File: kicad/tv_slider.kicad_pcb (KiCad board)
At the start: 2 copper layers, 100.6 x 75.2 mm, 95 parts, among them J1 MC 1,5/2-G-3.81, J2 MC 1,5/6-G-3.81, J3 MC 1,5/4-G-3.81, J4 MC 1,5/3-G-3.81, J5 MC 1,5/3-G-3.81, J6 MC 1,5/3-G-3.81, J7 MC 1,5/3-G-3.81, J8 Conn_01x04, Q1 CSD19537Q3, Q2 BSS138, U1 TPS26632RGE, U2 LMR33610ADDAR, U3 LMR33610ADDAR, U4 ESP32-C6-DEVKITC-1-N8, U6 ISL3280ExHZ, U7 LS7184N-S, U8 ISL3280ExHZ, U9 DRV8452SPWPR

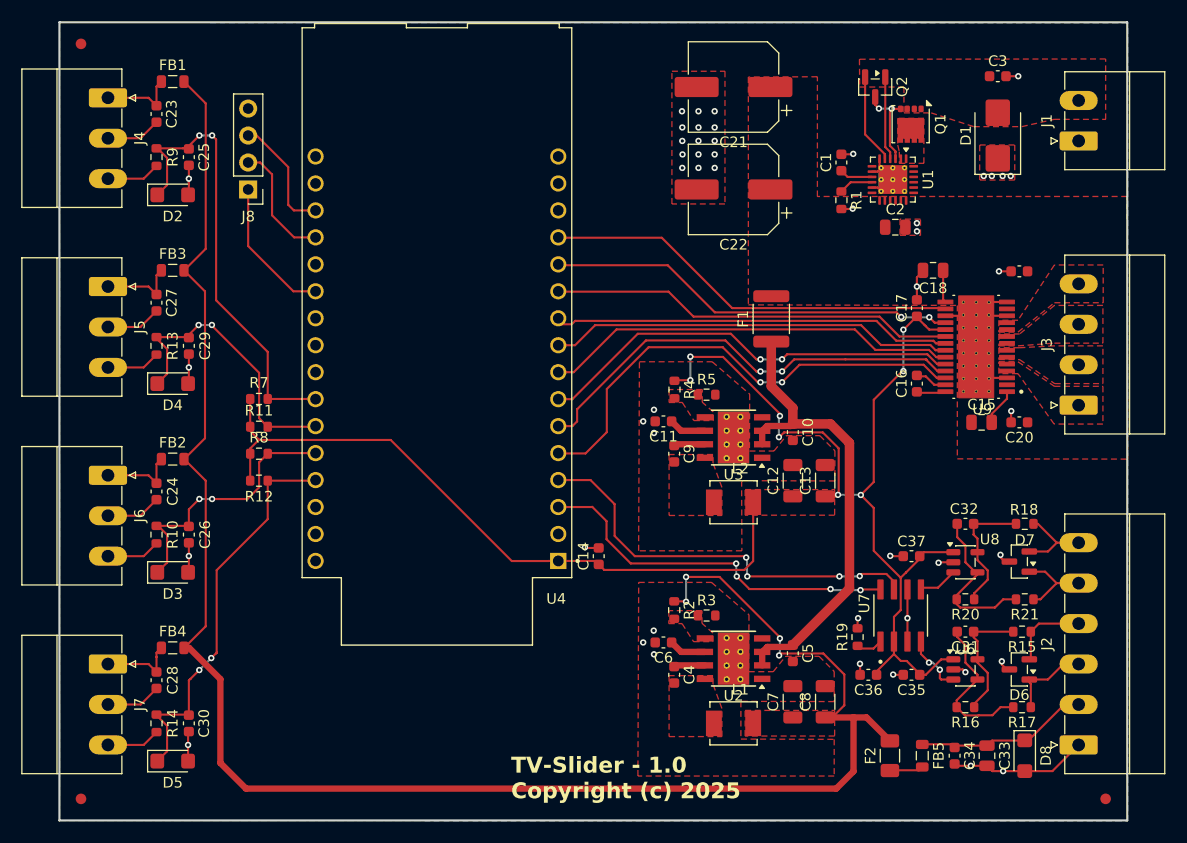
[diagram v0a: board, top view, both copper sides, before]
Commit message: Re-annotated and added extra capacitors for the 5V and 3V3 DC-DC converters. Added testpoints to the electronic fuse.
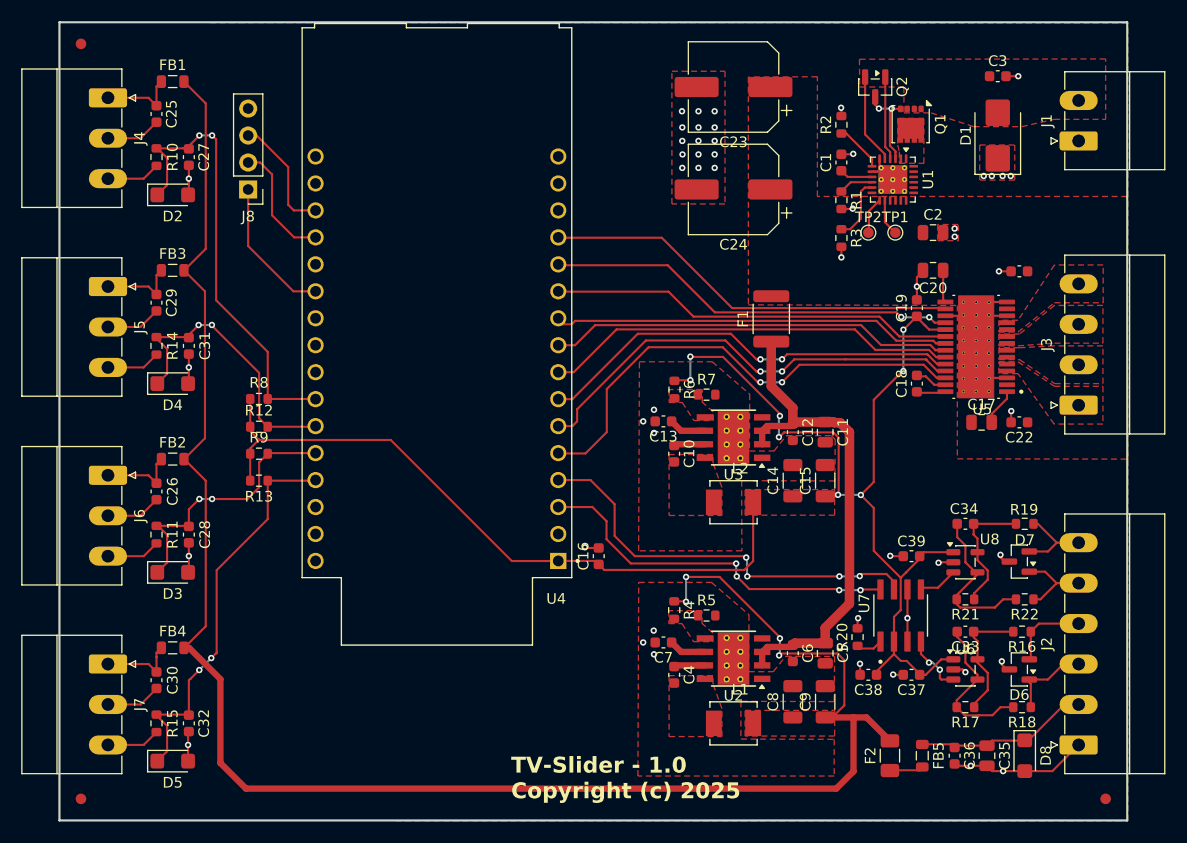
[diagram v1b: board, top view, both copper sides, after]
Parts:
- added C11: 4.7u, Capacitor_SMD:C_0805_2012Metric, F.Cu at (153.9, 95.0)
- added C5: 4.7u, Capacitor_SMD:C_0805_2012Metric, F.Cu at (153.9, 115.8)
- added R2: 0, Resistor_SMD:R_0603_1608Metric, F.Cu at (155.4, 66.0)
- added R3: 0, Resistor_SMD:R_0603_1608Metric, F.Cu at (155.4, 76.7)
- added TP1: ~{FLT}, TestPoint:TestPoint_Pad_D1.0mm, F.Cu at (160.5, 76.2)
- added TP2: IMON, TestPoint:TestPoint_Pad_D1.0mm, F.Cu at (158.0, 76.2)
- F1: value 300mA -> 100mA
- R1: value 6.98k -> 9.09k
- moved C2 3.59 mm to (164.1, 76.2)
- renumbered C9 to C10, C10 to C12, C11 to C13, C12 to C14, C13 to C15, C14 to C16, C15 to C17, C16 to C18, C17 to C19, C18 to C20, C19 to C21, C20 to C22, C21 to C23, C22 to C24, C23 to C25, C24 to C26, C25 to C27, C26 to C28, C27 to C29, C28 to C30, C29 to C31, C30 to C32, C31 to C33, C32 to C34, C33 to C35, C34 to C36, C35 to C37, C36 to C38, C37 to C39, C5 to C6, C6 to C7, C7 to C8, C8 to C9, R9 to R10, R10 to R11, R11 to R12, R12 to R13, R13 to R14, R14 to R15, R15 to R16, R16 to R17, R17 to R18, R18 to R19, R19 to R20, R20 to R21, R21 to R22, R2 to R4, R3 to R5, R4 to R6, R5 to R7, R7 to R8, R8 to R9, U9 to U5
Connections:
- U1 pad 11: GND -> Net-(U1-MODE)
- U1 pad 13: unconnected-(U1-IMON-Pad13) -> Net-(U1-IMON)
- U1 pad 14: unconnected-(U1-~{FLT}-Pad14) -> Net-(U1-~{FLT})
- U1 pad 7: unconnected-(U1-PLIM-Pad7) -> Net-(U1-PLIM)
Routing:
- net Net-(U1-MODE): track 0.00 -> 6.00 mm
- net Net-(U1-PLIM): track 0.00 -> 4.56 mm
- net Net-(U1-IMON): track 0.00 -> 3.47 mm
- net Net-(U1-~{FLT}): track 0.00 -> 3.44 mm
- net Net-(U2-EN): track 44.8 -> 47.2 mm
- net +5V: track 173.1 -> 173.8 mm
- net GND: track 80.0 -> 80.7 mm, vias 49 -> 51
- net +3V3: track 153.6 -> 154.2 mm

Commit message: Fixed up or explained all DRC violations.
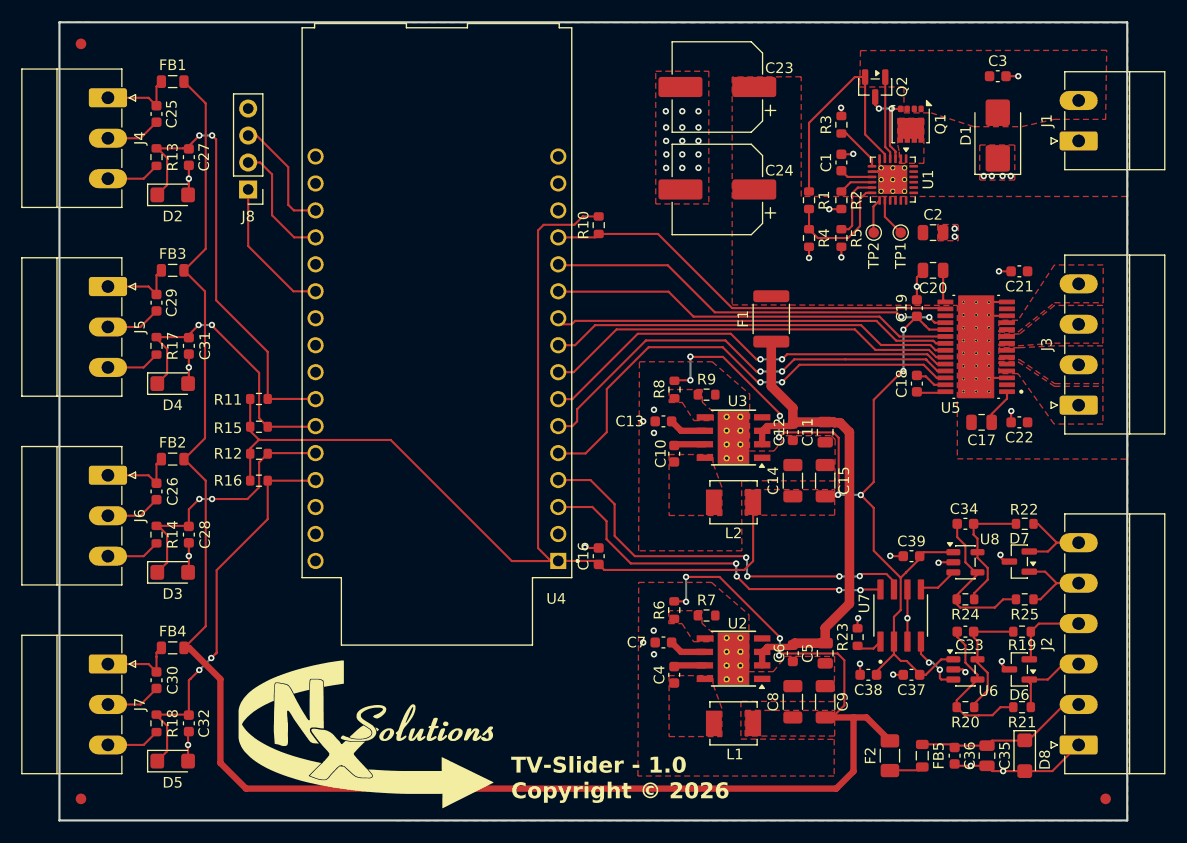
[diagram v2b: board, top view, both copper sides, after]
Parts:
- added R1: 1M, Resistor_SMD:R_0603_1608Metric, F.Cu at (152.4, 73.2)
- added R10: 10k, Resistor_SMD:R_0603_1608Metric, F.Cu at (132.6, 75.5)
- added R4: 150k, Resistor_SMD:R_0603_1608Metric, F.Cu at (152.4, 76.7)
- moved C23 1.52 mm to (143.8, 62.5)
- moved C24 1.52 mm to (143.8, 72.1)
- moved TP1 0.51 mm to (161.0, 76.2)
- moved TP2 0.51 mm to (158.5, 76.2)
- renumbered R8 to R11, R9 to R12, R10 to R13, R11 to R14, R12 to R15, R13 to R16, R14 to R17, R15 to R18, R16 to R19, R1 to R2, R17 to R20, R18 to R21, R19 to R22, R20 to R23, R21 to R24, R22 to R25, R2 to R3, R3 to R5, R4 to R6, R5 to R7, R6 to R8, R7 to R9
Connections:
- net Net-(U2-EN) renamed /Power supply/+24V_PROT
- U1 pad 12: unconnected-(U1-~{SHDN}-Pad12) -> Net-(U1-~{SHDN})
- U5 pad 17: GND -> unconnected-(U5-VREF-Pad17)
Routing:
- net +3V3: track 154.2 -> 192.3 mm
- net /Power supply/Vin: track 8.47 -> 22.0 mm
- net Net-(U1-~{SHDN}): track 0.00 -> 11.4 mm
- net GND: track 80.7 -> 79.5 mm, vias 51 -> 52
- net /Shaft encoder/A-: track 9.00 -> 8.29 mm
- net /Shaft encoder/B-: track 8.52 -> 7.90 mm
- net /MCU/~{FAULT}: track 39.0 -> 39.5 mm
- net Net-(J8-Pin_2): track 12.1 -> 11.5 mm
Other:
- board text added: "TV-Slider - 1.0 Copyright © 2026"
- board text removed: "TV-Slider - 1.0 Copyright (c) 2025"

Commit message: Reviewed the ESP32-C6-DEVKIT GPIO's. Some of them have a dual function and are better left untouched.
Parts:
- J8: value Conn_01x04 -> Conn_01x05; footprint Connector_PinHeader_2.54mm:PinHeader_1x04_P2.54mm_Vertical -> Connector_PinHeader_2.54mm:PinHeader_1x05_P2.54mm_Vertical
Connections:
- J8 pad 4: GND -> +3V3
- U4 pad J1_6: /MCU/ENABLE -> /MCU/DIR
- U4 pad J1_7: /MCU/DIR -> /MCU/STEP
- U4 pad J1_8: /MCU/STEP -> /MCU/SCLK
- U4 pad J1_9: /MCU/SCLK -> unconnected-(U4-GPIO8-PadJ1_9)
- U4 pad J3_10: unconnected-(U4-GPIO18-PadJ3_10) -> Net-(J8-Pin_3)
- U4 pad J3_11: Net-(J8-Pin_1) -> unconnected-(U4-GPIO9-PadJ3_11)
- U4 pad J3_13: Net-(J8-Pin_2) -> unconnected-(U4-GPIO13-PadJ3_13)
- U4 pad J3_14: Net-(J8-Pin_3) -> unconnected-(U4-GPIO12-PadJ3_14)
- U4 pad J3_8: unconnected-(U4-GPIO20-PadJ3_8) -> Net-(J8-Pin_1)
- U4 pad J3_9: unconnected-(U4-GPIO19-PadJ3_9) -> Net-(J8-Pin_2)
- U5 pad 25: /MCU/ENABLE -> +3V3
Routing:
- net +3V3: track 192.3 -> 236.0 mm, vias 8 -> 9
- net /MCU/ENABLE: track 42.3 -> 0.00 mm, vias 2 -> 0
- net Net-(J8-Pin_2): track 11.5 -> 21.9 mm
- net Net-(J8-Pin_3): track 11.4 -> 21.2 mm
- net Net-(J8-Pin_1): track 13.4 -> 21.6 mm
- net /MCU/DIR: track 40.3 -> 42.9 mm
- net /MCU/STEP: track 38.9 -> 40.8 mm
- net /MCU/SCLK: track 37.9 -> 39.3 mm
- net /MCU/UP/~{DOWN}: track 39.3 -> 39.9 mm
- net /MCU/MOSI: track 37.7 -> 37.1 mm
- net +5V: track 173.8 -> 174.3 mm
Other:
- board text added: "+"
- board text added: "12"
- board text added: "13"
- board text added: "3V3"
- board text added: "9"
- board text added: "ENCODER"
- board text added: "GND"
- board text added: "MOTOR"
- board text added: "VIN 24V"

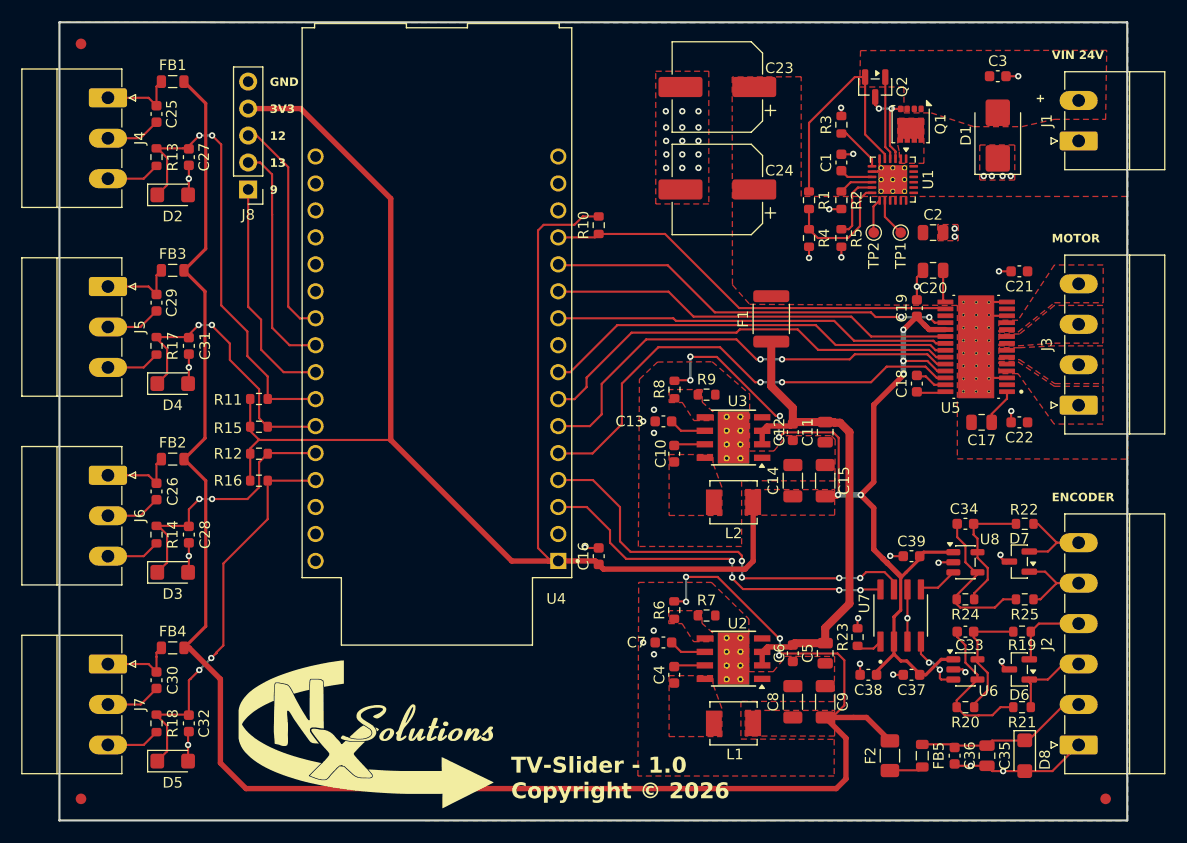
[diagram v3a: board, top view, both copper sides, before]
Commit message: Supplying the ESP32-C6-DEVKIT with 5V and using its 3V3 output to supply the boards logic. Removed the 3V3 switch mode power supply on the board.
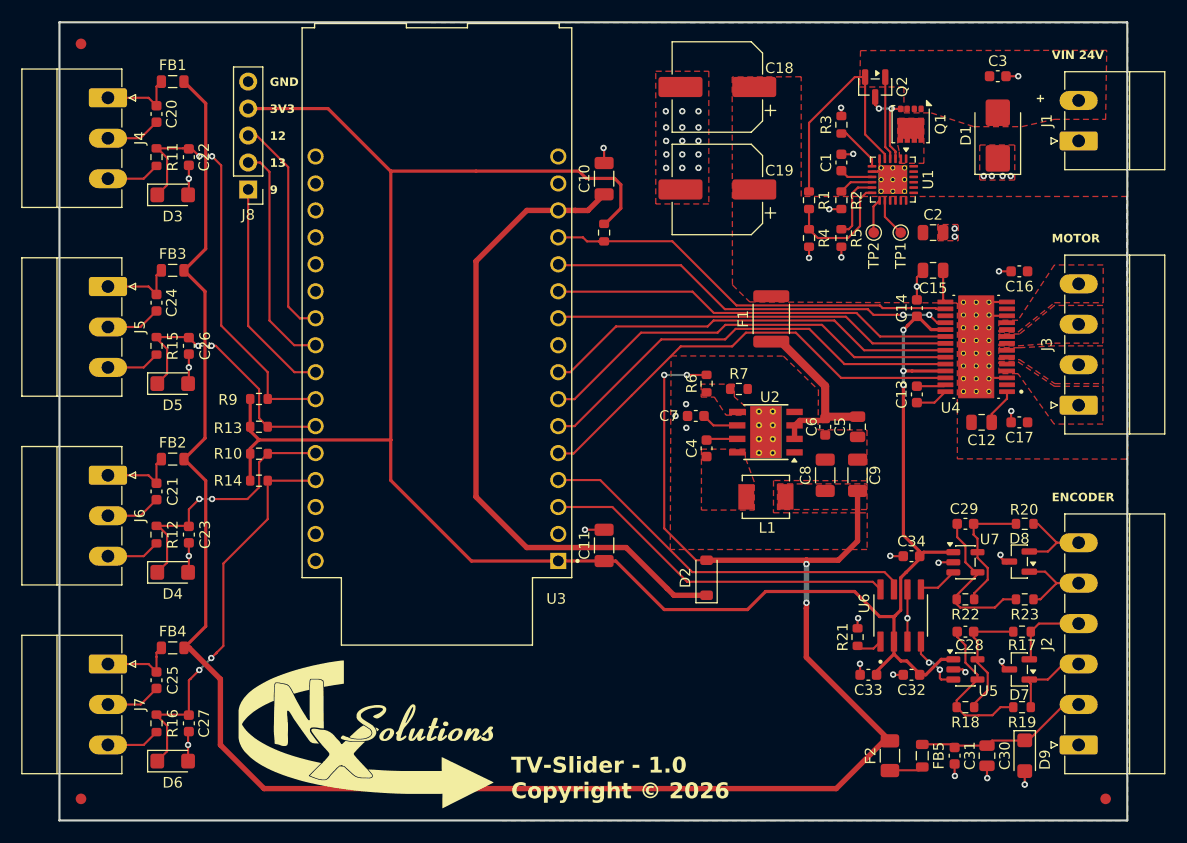
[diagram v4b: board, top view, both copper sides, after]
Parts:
- removed the C12 at (150.9, 95.0)
- removed the C13 at (138.7, 94.0)
- removed the C14 at (150.9, 99.6)
- removed the C15 at (153.9, 99.6)
- removed the C16 at (132.6, 106.7)
- removed L2: 10u, local_library:IND_SRP4020TA-100M
- removed the R8 at (139.7, 91.0)
- removed the R9 at (142.7, 91.5)
- removed the U3 at (145.3, 95.5)
- added D2: 1N5819HW-7-F, Diode_SMD:D_SOD-123, F.Cu at (142.7, 108.7)
- C10: value 100n -> 22u; footprint Capacitor_SMD:C_0603_1608Metric -> Capacitor_SMD:C_1206_3216Metric
- C11: value 4.7u -> 22u; footprint Capacitor_SMD:C_0805_2012Metric -> Capacitor_SMD:C_1206_3216Metric
- moved C10 26.7 mm to (133.1, 71.1), turned to 90 degrees
- moved C11 23.4 mm to (133.1, 105.7), turned to 90 degrees
- moved C7 21.6 mm to (141.7, 93.5)
- moved C4 21.6 mm to (142.7, 96.5)
- moved C5 21.6 mm to (157.0, 94.5)
- moved C6 21.6 mm to (153.9, 94.5)
- moved C8 21.6 mm to (153.9, 99.1)
- moved C9 21.6 mm to (157.0, 99.1)
- moved L1 21.6 mm to (148.3, 101.1)
- moved R6 21.6 mm to (142.7, 90.4)
- moved R7 21.6 mm to (145.8, 90.9)
- moved U2 21.6 mm to (148.3, 95.0)
- moved C13 1.02 mm to (162.6, 91.4)
- moved R8 0.86 mm to (133.1, 76.2)
- renumbered C17 to C12, C18 to C13, C19 to C14, C20 to C15, C21 to C16, C22 to C17, C23 to C18, C24 to C19, C25 to C20, C26 to C21, C27 to C22, C28 to C23, C29 to C24, C30 to C25, C31 to C26, C32 to C27, C33 to C28, C34 to C29, C35 to C30, C36 to C31, C37 to C32, C38 to C33, C39 to C34, D2 to D3, D3 to D4, D4 to D5, D5 to D6, D6 to D7, D7 to D8, D8 to D9, R12 to R10, R13 to R11, R14 to R12, R15 to R13, R16 to R14, R17 to R15, R18 to R16, R19 to R17, R20 to R18, R21 to R19, R22 to R20, R23 to R21, R24 to R22, R25 to R23, R10 to R8, R11 to R9, U4 to U3, U5 to U4, U6 to U5, U7 to U6, U8 to U7
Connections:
- C10 pad 1: Net-(U3-BOOT) -> Net-(D2-K)
- C10 pad 2: Net-(U3-SW) -> GND
- C11 pad 1: /Power supply/+24V_PROT -> +3V3
- U3 pad J1_14: unconnected-(U4-VCC_5V-PadJ1_14) -> Net-(D2-K)
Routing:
- net Net-(D2-K): track 0.00 -> 62.4 mm
- net +3V3: track 236.0 -> 200.9 mm, vias 9 -> 3
- net /Power supply/+24V_PROT: track 47.2 -> 17.4 mm
- net +5V: track 174.3 -> 200.2 mm
- net GND: track 79.5 -> 72.9 mm, vias 52 -> 51
- net /MCU/UP/~{DOWN}: track 39.9 -> 36.3 mm, vias 4 -> 0
- net Net-(U3-VCC): track 3.50 -> 0.00 mm
- net Net-(U3-BOOT): track 2.94 -> 0.00 mm
- net /Location sensors/OUT_STOP: track 42.7 -> 40.3 mm
- net /MCU/~{SLEEP}: track 45.0 -> 42.7 mm, vias 2 -> 0
- net /Location sensors/OUT_SLOW: track 27.4 -> 25.3 mm
- net /MCU/COUNT: track 35.3 -> 33.6 mm, vias 4 -> 0
- net /MCU/DIR: track 42.9 -> 41.6 mm, vias 2 -> 0
- net /MCU/MOSI: track 37.1 -> 37.9 mm
- net Net-(J8-Pin_1): track 21.6 -> 21.0 mm
- removed copper zone on F.Cu, net +3V3
- removed copper zone on F.Cu, net Net-(U3-FB)
- removed copper zone on F.Cu, net Net-(U3-SW)

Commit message: Added extra copper for cooling the DRV8452SPWPR motor driver.
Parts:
- moved FID1 97.0 mm to (180.8, 57.9)
- moved C12 2.54 mm to (171.2, 94.0), turned to 90 degrees
- moved C17 2.09 mm to (173.7, 95.5), turned to -90 degrees
- moved C16 1.02 mm to (171.2, 79.8)
- moved C15 1.02 mm to (165.1, 79.8), turned to 0 degrees
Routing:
- net GND: track 72.9 -> 69.8 mm, vias 51 -> 52
- net Net-(U4-VCP): track 3.48 -> 1.91 mm
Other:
- board text added: "IN_SLOW"
- board text added: "IN_STOP"
- board text added: "OUT_SLOW"
- board text added: "OUT_STOP"

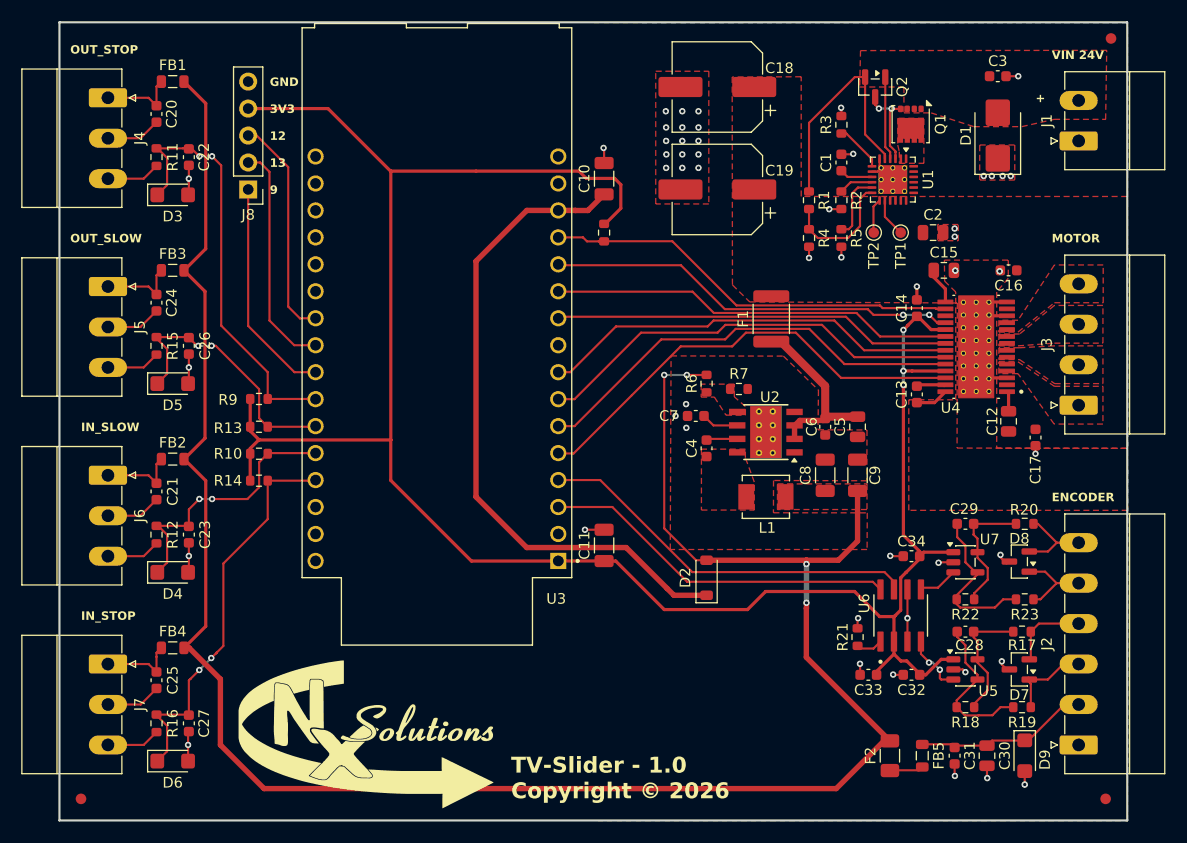
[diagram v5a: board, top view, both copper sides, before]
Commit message: Added some extra vias.
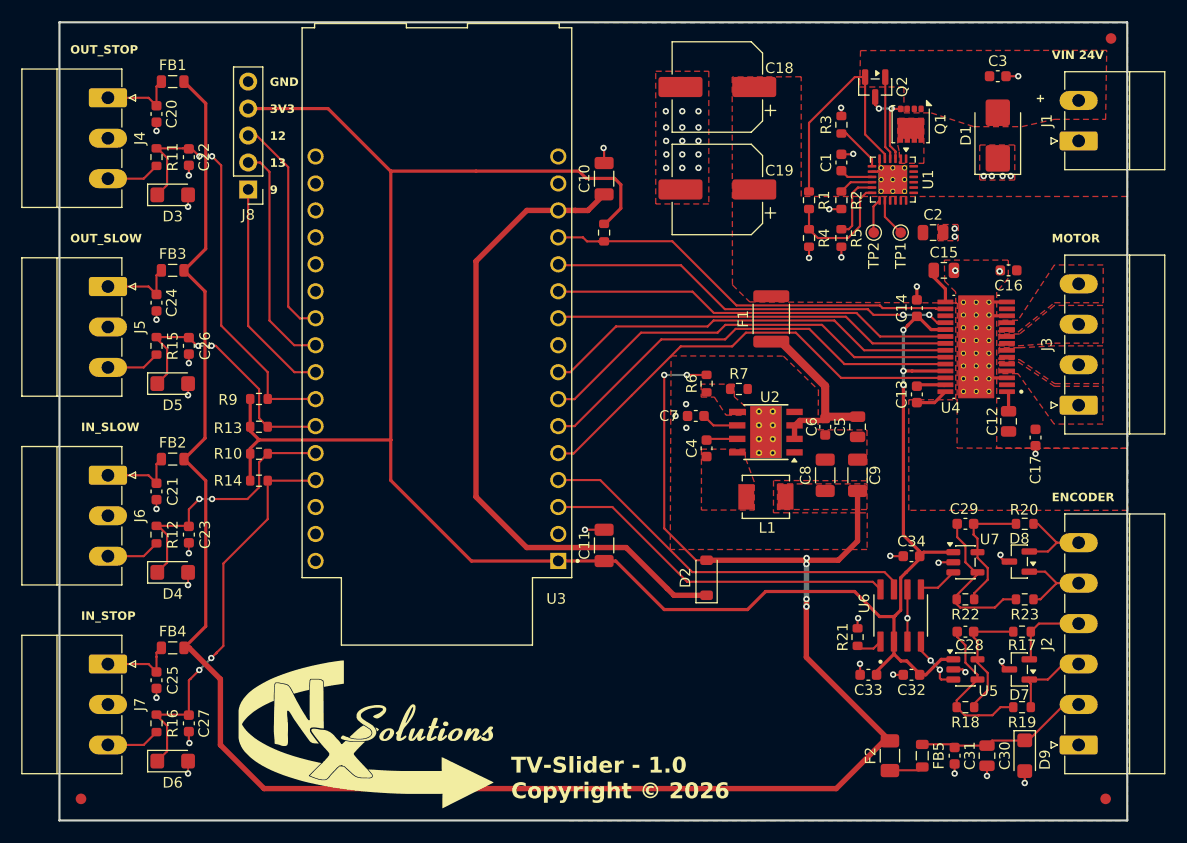
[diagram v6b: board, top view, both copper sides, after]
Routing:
- net GND: track 69.8 -> 48.9 mm, vias 52 -> 60
- net +5V: track 200.2 -> 201.5 mm, vias 4 -> 6
